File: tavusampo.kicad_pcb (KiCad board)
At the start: 2 copper layers, 1 part, among them U1 Z80CPU

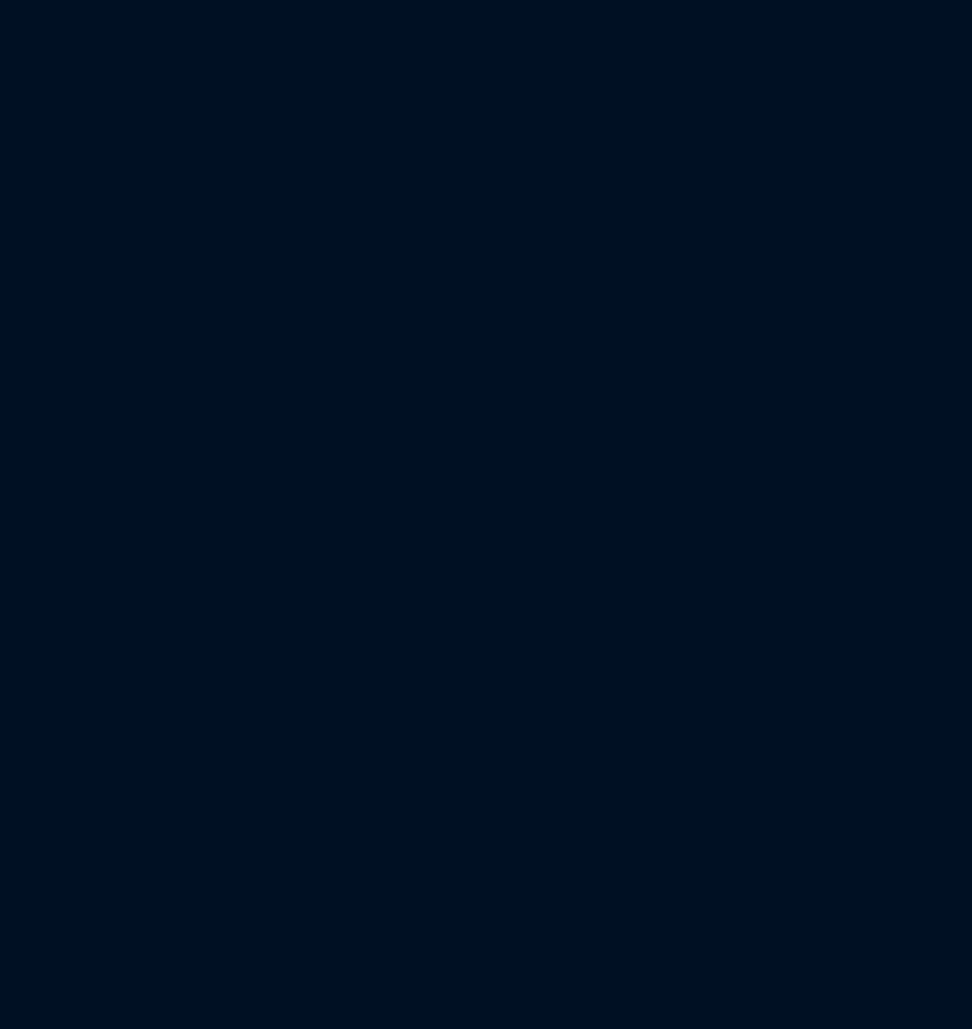
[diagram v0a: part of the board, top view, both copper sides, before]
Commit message: Fixed RAM pins
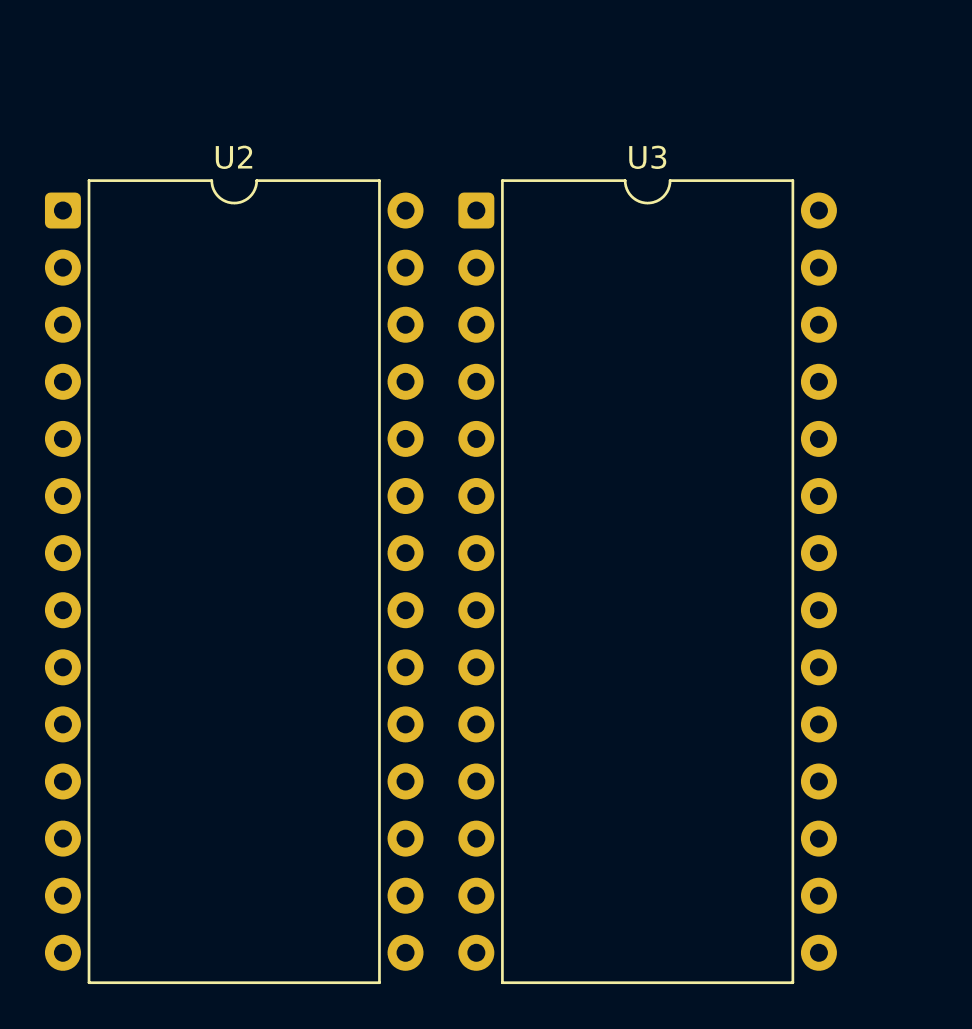
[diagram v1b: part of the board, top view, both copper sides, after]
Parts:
- added U2: CY62256LL-70PC, Package_DIP:DIP-28_W15.24mm, F.Cu at (70.9, 90.0)
- added U3: 27C512, Package_DIP:DIP-28_W15.24mm, F.Cu at (89.3, 90.0)

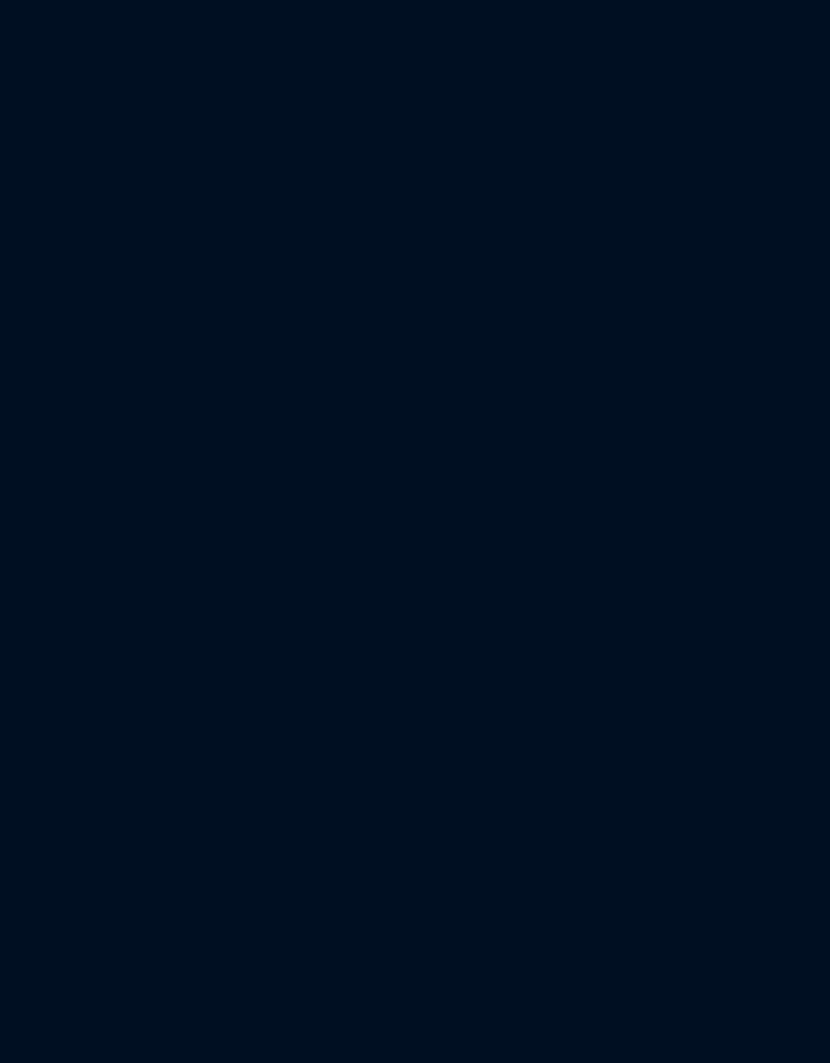
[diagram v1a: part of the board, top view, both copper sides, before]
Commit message: added some displays
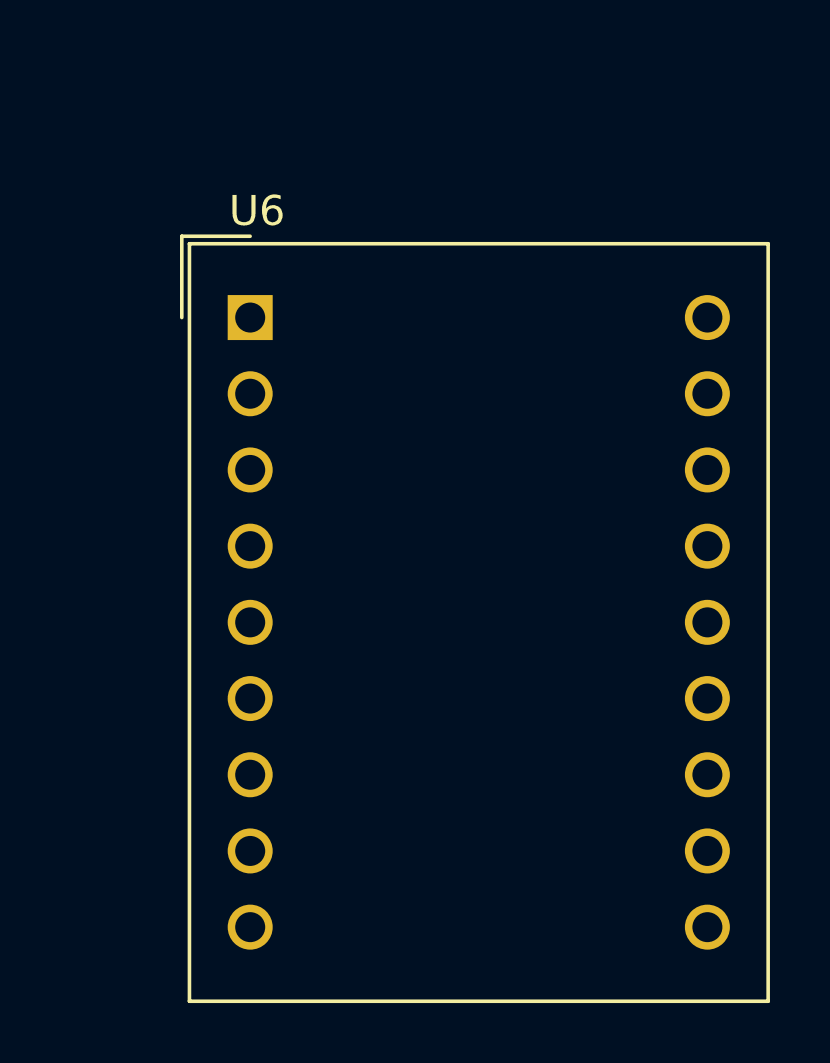
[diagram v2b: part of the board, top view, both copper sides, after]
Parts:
- added U6: HDSP-523E, Display_7Segment:DA56-11SURKWA, F.Cu at (195.8, 117.7)
